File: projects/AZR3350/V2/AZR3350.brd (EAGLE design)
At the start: 128 x 80.5 mm, 188 parts, among them IC1 LM2734Y, IC10 A4988, IC2 LDO-TS1117CW-3V3, IC3 ATSAM4S8C, IC4 SI87XXIS, IC5 74HC125, IC6 74S08D, IC7 A4988, IC8 A4988, IC9 A4988, J1 ZX62-AB-5PA, J3 MSTBV4, J4 MOLEX-105162-001, Q1 NX138BKS, Q2 BUK9Y53-100B, Q3 BUK9Y53-100B, X1 12MHz

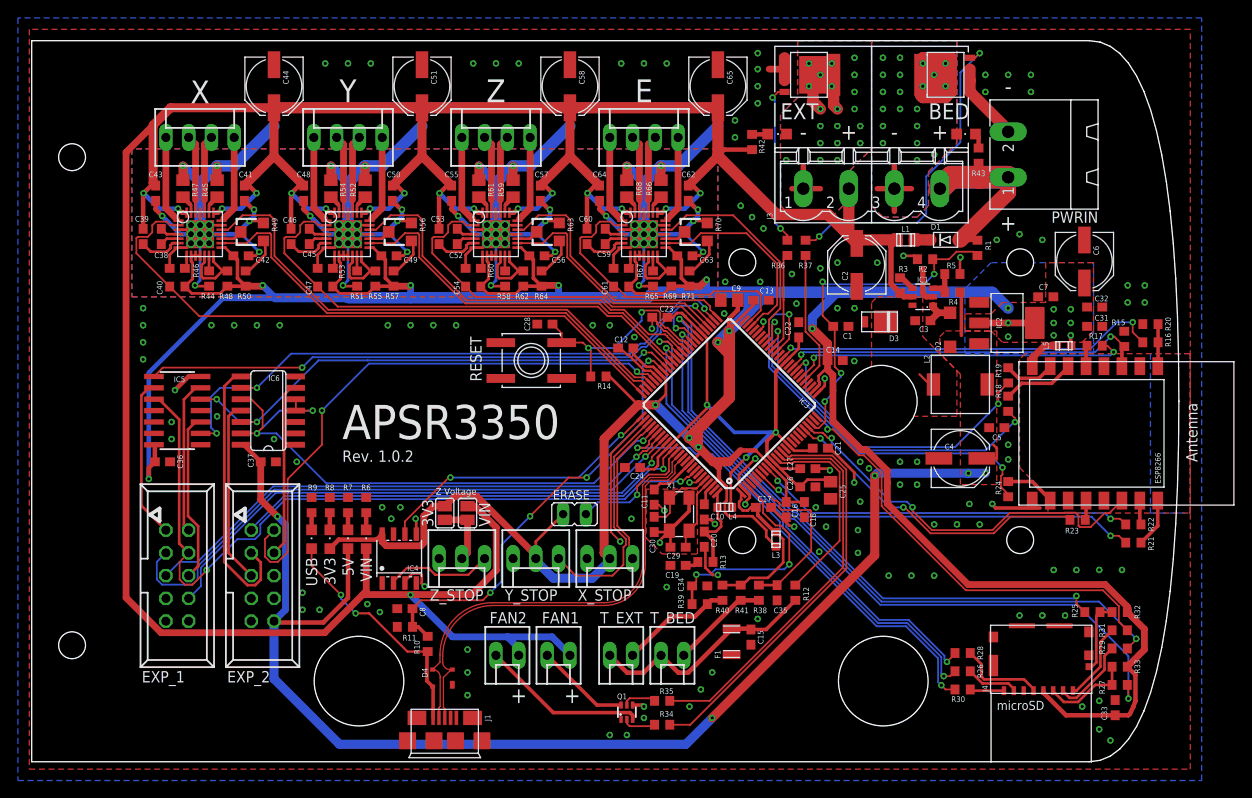
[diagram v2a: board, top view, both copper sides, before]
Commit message: LCD screen
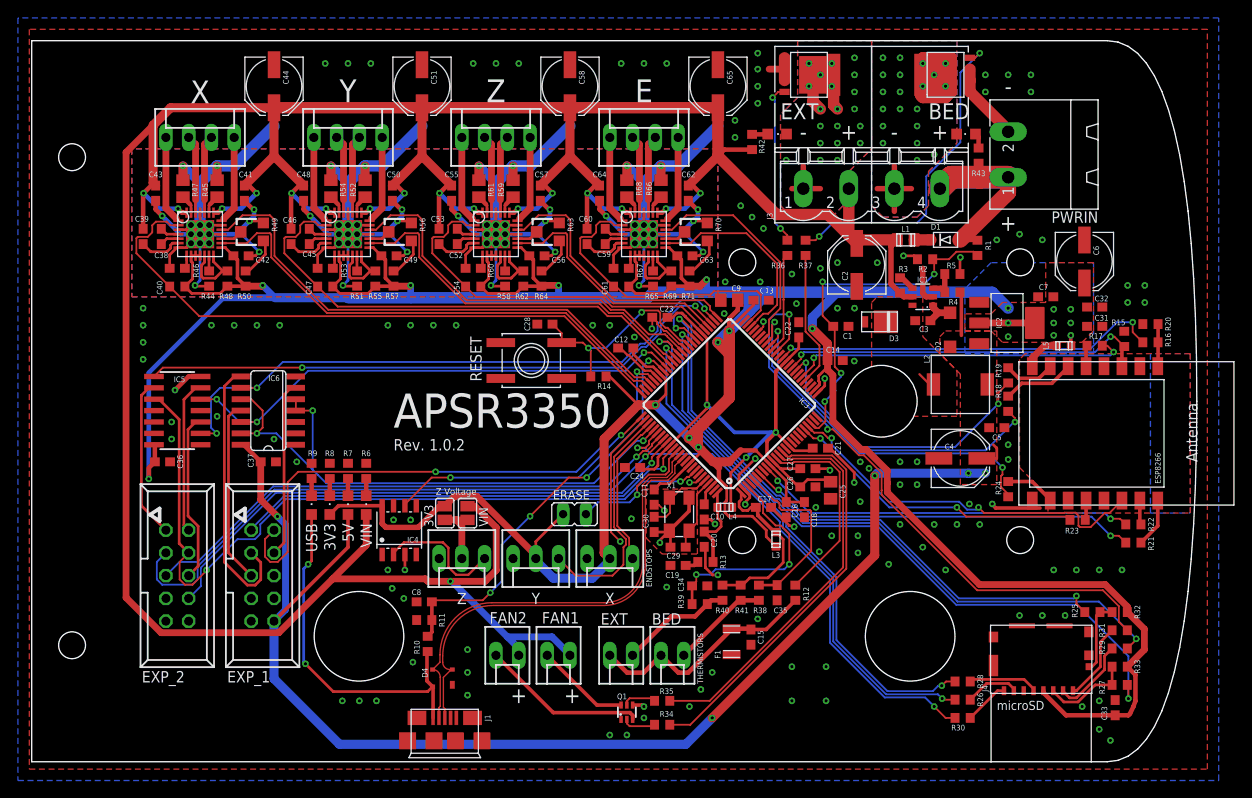
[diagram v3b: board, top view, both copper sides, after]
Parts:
- moved EXP_1 9.52 mm to (-74.3, -34.3)
- moved EXP_2 9.52 mm to (-83.8, -34.3)
- moved 3V3 3.81 mm to (-66.8, -26.4)
- moved 5V 3.81 mm to (-64.8, -26.4)
- moved R6 3.81 mm to (-62.7, -22.6)
- moved R7 3.81 mm to (-64.8, -22.6)
- moved R8 3.81 mm to (-66.8, -22.6)
- moved R9 3.81 mm to (-68.8, -22.6)
- moved USB 3.81 mm to (-68.8, -26.4)
- moved VIN 3.81 mm to (-62.7, -26.4)
- moved R26 3.18 mm to (3.81, -48.1)
- moved IC4 3.17 mm to (-59.1, -29.2)
- moved R28 3.17 mm to (3.81, -46.1)
- moved R30 3.17 mm to (3.81, -50.2)
- moved C8 2.29 mm to (-56.3, -37.2)
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- renumbered T_BED to BED, T_EXT to EXT
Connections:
- net +5V: now also EXP_1.10; no longer EXP_2.10
- net BEEPER: now also EXP_1.1; no longer EXP_2.1
- net BTN_EN1: now also EXP_2.5; no longer EXP_1.5
- net BTN_EN2: now also EXP_2.3; no longer EXP_1.3
- net BTN_ENC: now also EXP_1.2; no longer EXP_2.2
- net LCD_CS_BUF: now also EXP_1.4; no longer EXP_2.4
- net LCD_MISO_BUF: now also EXP_2.1; no longer EXP_1.1
- net LCD_MOSI_BUF: now also EXP_1.3; no longer EXP_2.3
- net LCD_RST: now also EXP_2.8; no longer EXP_1.8
- net LCD_SCK_BUF: now also EXP_1.5; no longer EXP_2.5
- net LCD_SD_CS: now also EXP_2.4; no longer EXP_1.4
- net SD_MOSI_BUF: now also EXP_2.6; no longer EXP_1.6
- net SD_SCK_BUF: now also EXP_2.2; no longer EXP_1.2
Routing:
- net VBUS: track 26.9 -> 40.6 mm
- net MCCK: track 55.8 -> 61.0 mm
- net GND: track 383.6 -> 379.7 mm, vias 198 -> 203
- net MCDA0: track 54.4 -> 58.3 mm
- net MCDA1: track 51.8 -> 55.7 mm
- net USB_PWR_MON: track 50.1 -> 47.5 mm
- net +3V3: track 468.6 -> 466.1 mm
- net Z_STOP_IN: track 12.0 -> 14.3 mm
- net Z_STOP: track 32.6 -> 30.6 mm
- net CLK: track 9.74 -> 7.81 mm
- net ESP_DATA_RDY: track 35.8 -> 34.3 mm
- net SAM_TFR_RDY: track 43.7 -> 42.3 mm
- net DAT1: track 3.82 -> 5.02 mm
- net +24V: track 379.7 -> 378.9 mm
- net MCDA2: track 68.2 -> 67.4 mm
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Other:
- board size 128 x 80.5 mm -> 130 x 80.5 mm
- board text added: "ENDSTOPS"
- board text added: "THERMISTORS"
- board text added: "X"
- board text added: "Y"
- board text added: "Z"
